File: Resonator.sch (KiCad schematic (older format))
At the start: 7 parts, among them U1 PCM3060

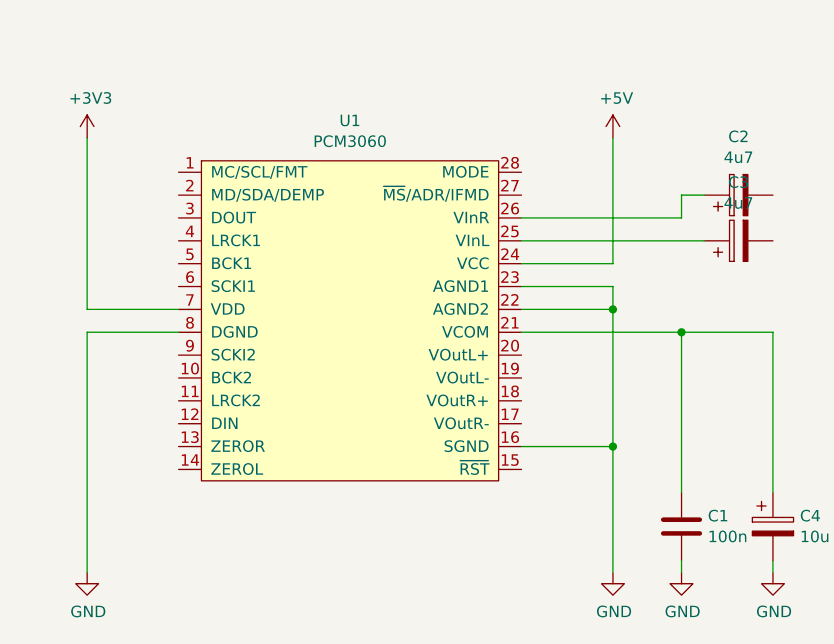
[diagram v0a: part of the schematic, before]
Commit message: More work on basic configuraiton of CODEC.
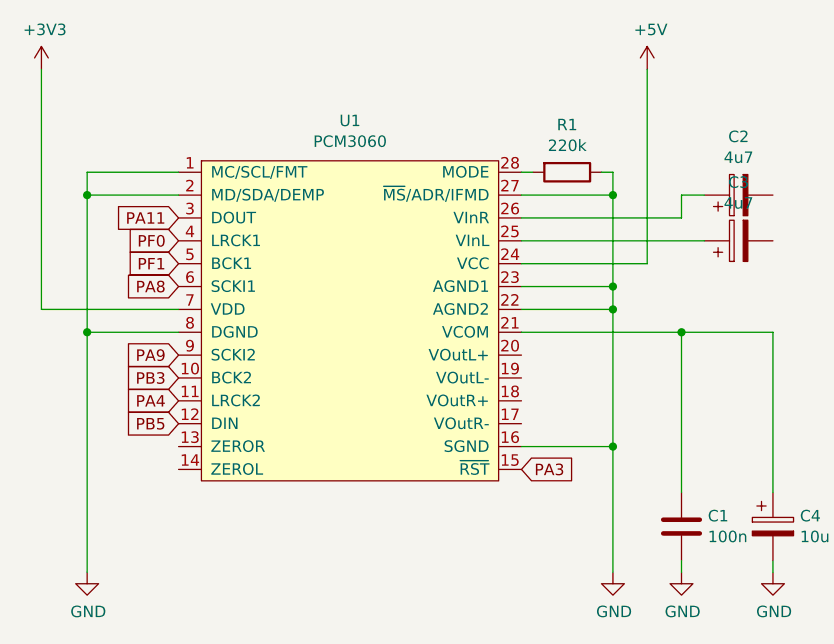
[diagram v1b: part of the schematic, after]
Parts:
- added R1: 220k, symbol Device:R
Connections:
- net GND: now also U1.1 (MC/SCL/FMT), U1.2 (MD/SDA/DEMP), U1.27 (~MS~/ADR/IFMD), R1.1
- net PB3: now reaches U1.10 (BCK2)
- net PA4: now reaches U1.11 (LRCK2)
- net PB5: now reaches U1.12 (DIN)
- net PA3: now reaches U1.15 (~RST)
- net at U1.28 (MODE): now also R1.2
- net PA11: now reaches U1.3 (DOUT)
- net PF0: now reaches U1.4 (LRCK1)
- net PF1: now reaches U1.5 (BCK1)
- net PA8: now reaches U1.6 (SCKI1)
- net PA9: now reaches U1.9 (SCKI2)
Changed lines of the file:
@@
 $EndDescr
-$Comp
-L PCM3060:PCM3060 U1
-U 1 1 619A1A69
-P 5250 3000
-F 0 "U1" H 5200 3825 50  0000 C CNN
-F 1 "PCM3060" H 5200 3734 50  0000 C CNN
-F 2 "Package_SO:TSSOP-28_4.4x9.7mm_P0.65mm" H 5250 3000 50  0001 C CNN
-F 3 "https://www.ti.com/lit/gpn/pcm3060" H 5250 3000 50  0001 C CNN
-F 4 "Texas Instruments" H 5250 3000 50  0001 C CNN "Manufacturer"
-	1    5250 3000
-	1    0    0    -1
-$EndComp
 $Comp
 L power:+3V3 #PWR01
 U 1 1 619A5D1A
-P 4050 2250
-F 0 "#PWR01" H 4050 2100 50  0001 C CNN
-F 1 "+3V3" H 4065 2423 50  0000 C CNN
-F 2 "" H 4050 2250 50  0001 C CNN
-F 3 "" H 4050 2250 50  0001 C CNN
-	1    4050 2250
-	1    0    0    -1
-$EndComp
-Wire Wire Line
-	4050 2250 4050 3000
+P 3850 1950
+F 0 "#PWR01" H 3850 1800 50  0001 C CNN
+F 1 "+3V3" H 3865 2123 50  0000 C CNN
+F 2 "" H 3850 1950 50  0001 C CNN
+F 3 "" H 3850 1950 50  0001 C CNN
+	1    3850 1950
+	1    0    0    -1
+$EndComp
+Wire Wire Line
+	3850 1950 3850 3000
 $Comp
 L power:+5V #PWR03
 U 1 1 619A9317
-P 6350 2250
-F 0 "#PWR03" H 6350 2100 50  0001 C CNN
-F 1 "+5V" H 6365 2423 50  0000 C CNN
-F 2 "" H 6350 2250 50  0001 C CNN
-F 3 "" H 6350 2250 50  0001 C CNN
-	1    6350 2250
-	1    0    0    -1
-$EndComp
-Wire Wire Line
-	6350 2250 6350 2800
+P 6500 1950
+F 0 "#PWR03" H 6500 1800 50  0001 C CNN
+F 1 "+5V" H 6515 2123 50  0000 C CNN
+F 2 "" H 6500 1950 50  0001 C CNN
+F 3 "" H 6500 1950 50  0001 C CNN
+	1    6500 1950
+	1    0    0    -1
+$EndComp
+Wire Wire Line
+	6500 1950 6500 2800
 $Comp
 L power:GND #PWR02
@@
 $EndComp
 Wire Wire Line
-	4050 3000 4450 3000
-Wire Wire Line
 	4050 3100 4450 3100
 Wire Wire Line
@@
 	5950 2700 6750 2700
 Wire Wire Line
-	5950 2800 6350 2800
+	5950 2800 6500 2800
 Wire Wire Line
 	5950 2900 6350 2900
@@
 Wire Wire Line
 	5950 3600 6350 3600
+Text GLabel 5950 3700 2    50   Input ~ 0
+PA3
+Text GLabel 4450 2600 0    50   Input ~ 0
+PA11
+Text GLabel 4450 2700 0    50   Input ~ 0
+PF0
+Text GLabel 4450 2800 0    50   Input ~ 0
+PF1
+Text GLabel 4450 2900 0    50   Input ~ 0
+PA8
+Text GLabel 4450 3200 0    50   Input ~ 0
+PA9
+Text GLabel 4450 3300 0    50   Input ~ 0
+PB3
+Text GLabel 4450 3400 0    50   Input ~ 0
+PA4
+Text GLabel 4450 3500 0    50   Input ~ 0
+PB5
+$Comp
+L PCM3060:PCM3060 U1
+U 1 1 619C61BC
+P 5250 3000
+F 0 "U1" H 5200 3825 50  0000 C CNN
+F 1 "PCM3060" H 5200 3734 50  0000 C CNN
+F 2 "Package_SO:TSSOP-28_4.4x9.7mm_P0.65mm" H 5250 3000 50  0001 C CNN
+F 3 "https://www.ti.com/lit/gpn/pcm3060" H 5250 3000 50  0001 C CNN
+F 4 "Texas Instruments" H 5250 3000 50  0001 C CNN "Manufacturer"
+	1    5250 3000
+	1    0    0    -1
+$EndComp
+Wire Wire Line
+	6350 2400 6350 2500
+Connection ~ 6350 2900
+Wire Wire Line
+	5950 2500 6350 2500
+Connection ~ 6350 2500
+Wire Wire Line
+	6350 2500 6350 2900
+$Comp
+L Device:R R1
+U 1 1 619D3A1C
+P 6150 2400
+F 0 "R1" V 5943 2400 50  0000 C CNN
+F 1 "220k" V 6034 2400 50  0000 C CNN
+F 2 "" V 6080 2400 50  0001 C CNN
+F 3 "~" H 6150 2400 50  0001 C CNN
+	1    6150 2400
+	0    1    1    0
+$EndComp
+Wire Wire Line
+	5950 2400 6000 2400
+Wire Wire Line
+	6300 2400 6350 2400
+Wire Wire Line
+	3850 3000 4450 3000
+Wire Wire Line
+	4450 2500 4050 2500
+Wire Wire Line
+	4050 2500 4050 3100
+Connection ~ 4050 3100
+Wire Wire Line
+	4050 2500 4050 2400
+Wire Wire Line
+	4050 2400 4450 2400
+Connection ~ 4050 2500
 $EndSCHEMATC

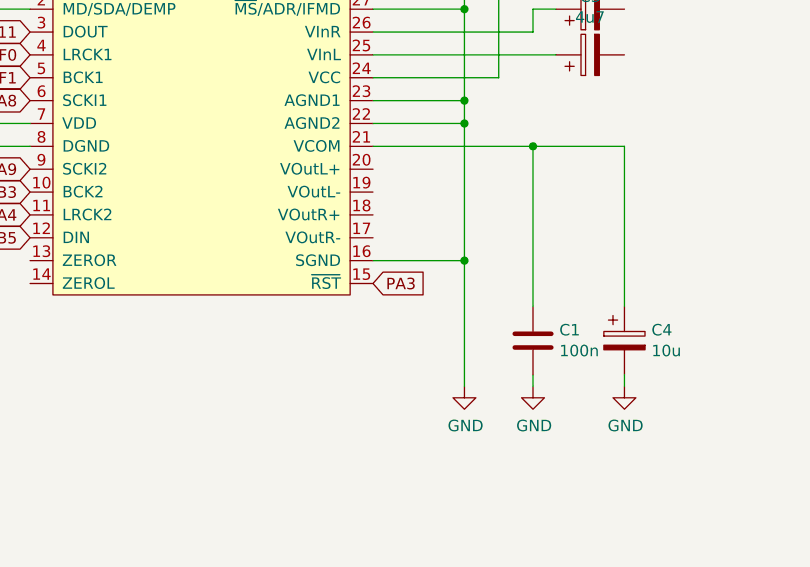
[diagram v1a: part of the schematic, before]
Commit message: Corrected reset pin assignment.
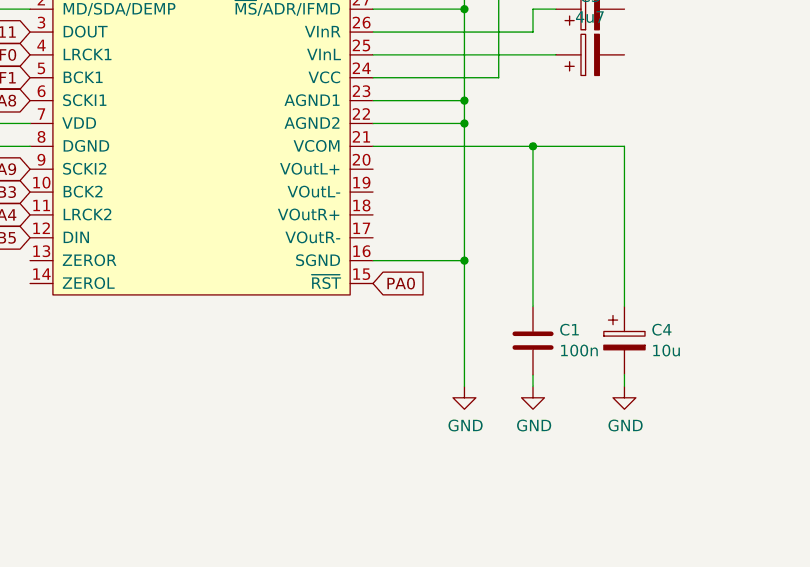
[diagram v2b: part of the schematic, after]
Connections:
- net PA3 renamed PA0
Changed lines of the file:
@@
 	5950 3600 6350 3600
 Text GLabel 5950 3700 2    50   Input ~ 0
-PA3
+PA0
 Text GLabel 4450 2600 0    50   Input ~ 0
 PA11

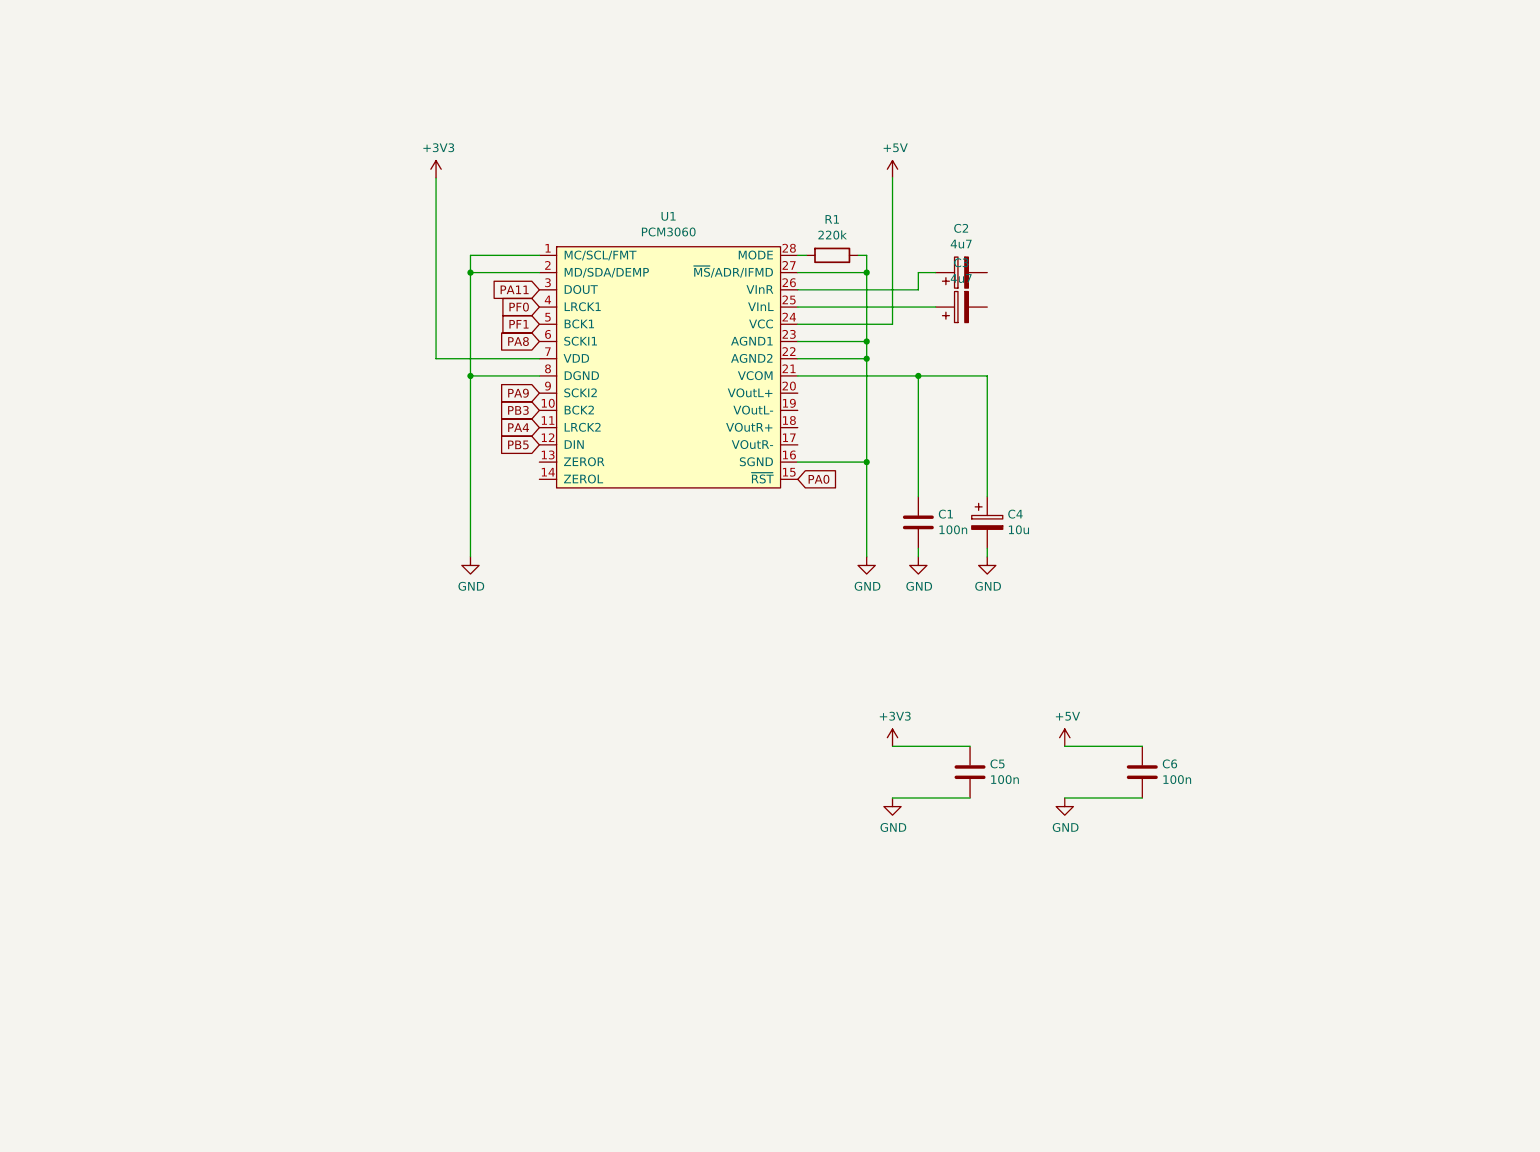
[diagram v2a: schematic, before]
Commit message: Added input stages to schema.
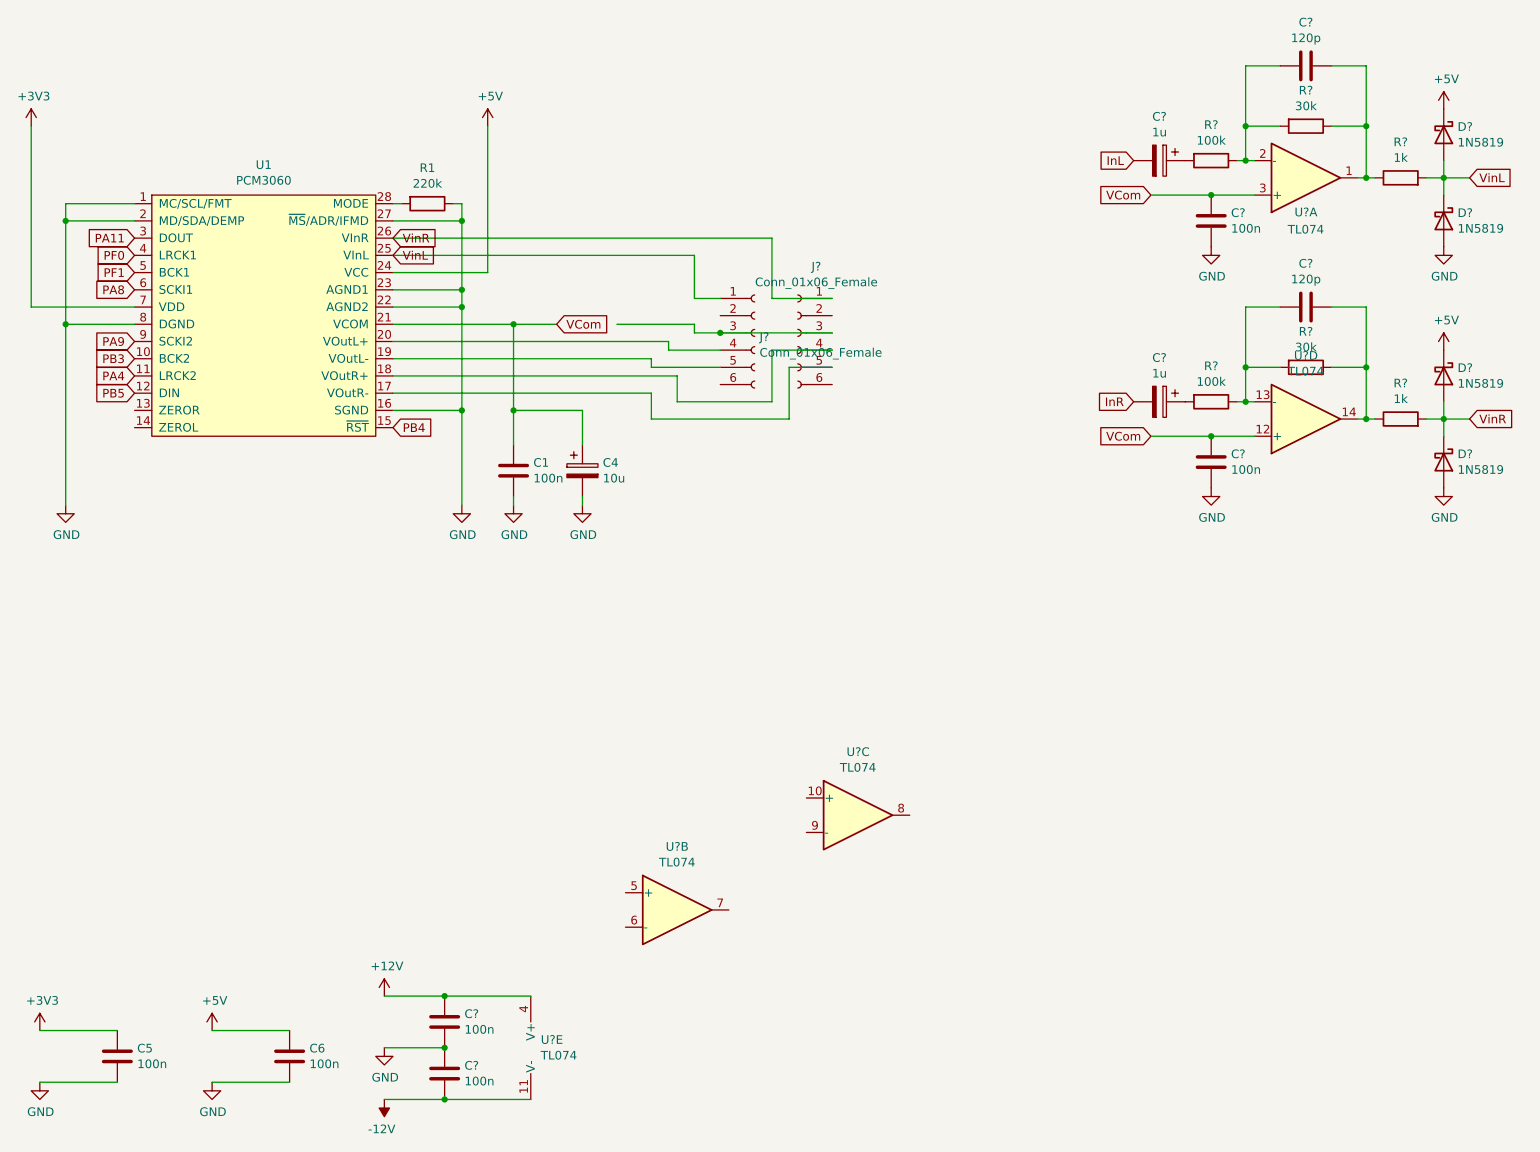
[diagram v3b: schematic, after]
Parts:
- removed C2, C3: 4u7, symbol Device:CP
- added C? (x2): 120p, symbol Device:C
- added C? (x4): 100n, symbol Device:C
- added C? (x2): 1u, symbol Device:CP
- added D? (x4): 1N5819, symbol Device:D_Schottky
- added J? (x2): Conn_01x06_Female, symbol Connector:Conn_01x06_Female
- added R? (x2): 100k, symbol Device:R
- added R? (x2): 1k, symbol Device:R
- added R? (x2): 30k, symbol Device:R
- added U? (x5): TL074, symbol Amplifier_Operational:TL074
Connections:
- net +5V: now also D?.1 (K), D?.1 (K)
- net GND: now also C?.1, C?.2, C?.2, C?.2, D?.2 (A), D?.2 (A)
- net VCom: now reaches C1.1, C4.1, U1.21 (VCOM)
- net VCom: now also C?.1, C?.1, U?.12 (+), U?.3 (+)
- net VinR: now reaches U1.26 (VInR)
- net VinR: now also D?.1 (K), D?.2 (A), J?.1 (Pin_1), R?.2
- net VinL: now reaches U1.25 (VInL)
- net VinL: now also D?.1 (K), D?.2 (A), J?.1 (Pin_1), R?.2
- net at U1.17 (VOutR-): now also J?.5 (Pin_5)
- net at U1.18 (VOutR+): now also J?.4 (Pin_4)
- net at U1.19 (VOutL-): now also J?.5 (Pin_5)
- net at U1.20 (VOutL+): now also J?.4 (Pin_4)
- net PA0 renamed PB4
- new net: C?.1, R?.1, R?.1, U?.1
- new net: C?.2, R?.1, R?.2, U?.2 (-)
- new net: C?.2, R?.1, R?.2, U?.13 (-)
- new net: C?.1, R?.1, R?.1, U?.14
- new net: C?.1, R?.2 (x2)
- new net: J?.3 (Pin_3), J?.3 (Pin_3)
- new net +12V: C?.1, U?.4 (V+)
- new net -12V: C?.2, U?.11 (V-)
- new net InL: C?.2
- new net InR: C?.2
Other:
- moved on the sheet: C1, C4, C5, C6, R1, U1
